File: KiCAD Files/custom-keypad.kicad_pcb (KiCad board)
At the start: 2 copper layers, 67.8 x 65.6 mm, 50 parts, among them IC1 AZ1117IH-3.3TRG1, IC2 USBLC6-2SC6, J1 UJ32-C-H-G-H2-SMT-TR, J2 EN11-HSM1BF20, J3 61300511121, SW1 SW_Push, SW2 SW_Push, SW3 SW_Push, SW4 SW_Push, SW8 SW_Push, SW9 SW_Push, U1 STM32H7A3RGTx, Y2 XRCGB25M000FAN00R0

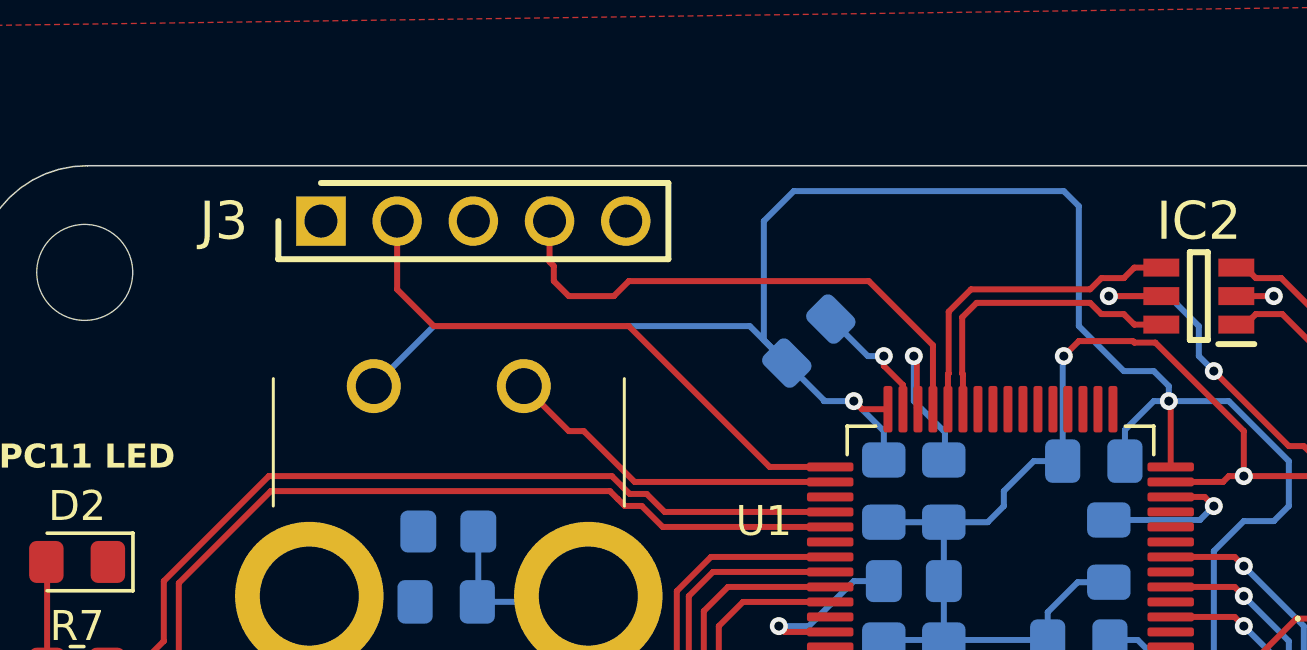
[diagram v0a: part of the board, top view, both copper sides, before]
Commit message: adjusted programming header location to provide more space to dial
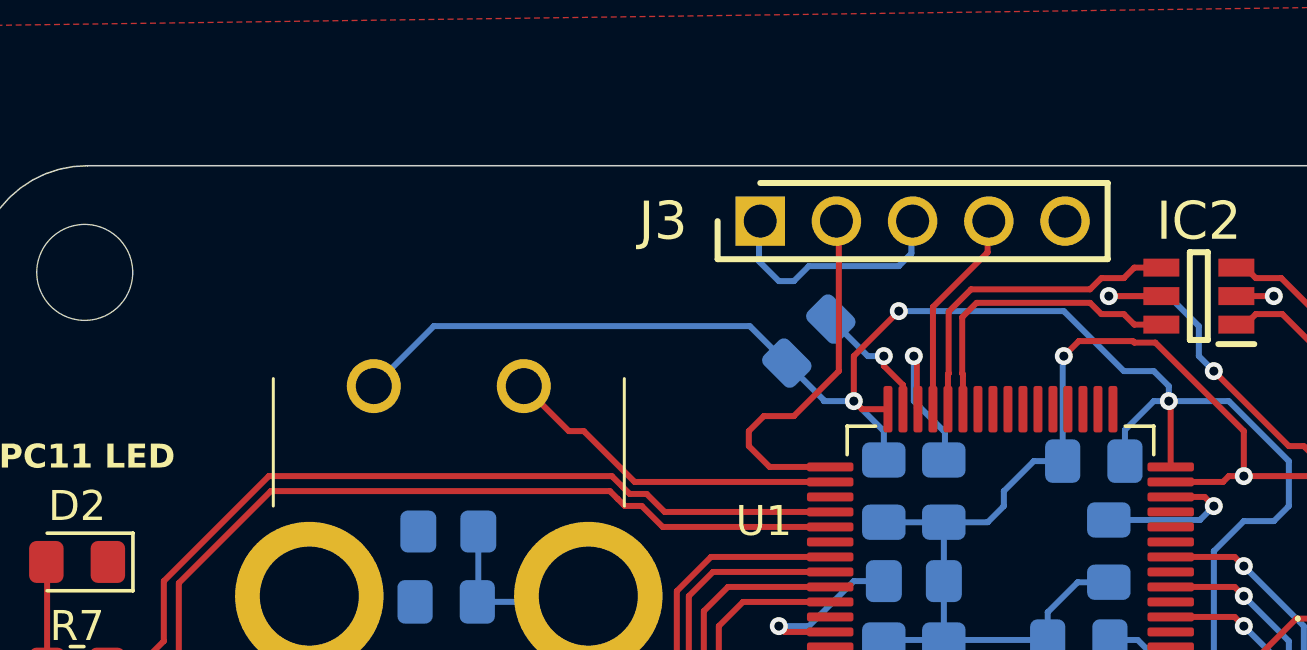
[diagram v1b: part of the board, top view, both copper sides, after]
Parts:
- moved J3 14.6 mm to (77.4, 27.5)
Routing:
- net PA13/SWDIO: track 18.1 -> 7.02 mm
- net VBAT: track 254.6 -> 244.3 mm, vias 7 -> 8
- net GND: track 146.5 -> 154.6 mm
- net PA14/SWCLK: track 19.2 -> 12.4 mm
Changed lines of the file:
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@@
 	(footprint "CustomFootprints:HDRV5W64P0X254_1X5_1270X254X854P"
 		(layer "F.Cu")
-		(at 62.738 27.5)
+		(at 77.38 27.5)
 		(descr "61300511121-1")
 		(tags "Connector")
@@
 	)
 	(segment
+		(start 78.5 29.5)
+		(end 78 29.5)
+		(width 0.2)
+		(layer "B.Cu")
+		(net 1)
+	)
+	(segment
 		(start 113.5 34)
 		(end 113.5 38)
@@
 	)
 	(segment
+		(start 78 29.5)
+		(end 77.34 28.84)
+		(width 0.2)
+		(layer "B.Cu")
+		(net 1)
+	)
+	(segment
 		(start 78 43.5)
 		(end 77.5 44)
@@
 	)
 	(segment
+		(start 82.42 27.5)
+		(end 82.42 28.58)
+		(width 0.2)
+		(layer "B.Cu")
+		(net 1)
+	)
+	(segment
 		(start 86.9625 40.5375)
 		(end 87.9625 39.5375)
@@
 	)
 	(segment
+		(start 79 29)
+		(end 78.5 29.5)
+		(width 0.2)
+		(layer "B.Cu")
+		(net 1)
+	)
+	(segment
 		(start 86.9625 46.4625)
 		(end 87 46.5)
@@
 	)
 	(segment
+		(start 82 29)
+		(end 79 29)
+		(width 0.2)
+		(layer "B.Cu")
+		(net 1)
+	)
+	(segment
 		(start 87.9625 39.5375)
 		(end 89 39.5375)
@@
 	)
 	(segment
+		(start 82.42 28.58)
+		(end 82 29)
+		(width 0.2)
+		(layer "B.Cu")
+		(net 1)
+	)
+	(segment
+		(start 77.34 28.84)
+		(end 77.34 27.5)
+		(width 0.2)
+		(layer "B.Cu")
+		(net 1)
+	)
+	(segment
 		(start 106.742 77.724)
 		(end 87.842 77.724)
@@
 	)
 	(segment
+		(start 80.5 32)
+		(end 80.5 33.5)
+		(width 0.2)
+		(layer "F.Cu")
+		(net 2)
+	)
+	(segment
 		(start 88.944213 47.233623)
 		(end 87.638 45.92741)
@@
 	)
 	(segment
+		(start 82 30.5)
+		(end 80.5 32)
+		(width 0.2)
+		(layer "F.Cu")
+		(net 2)
+	)
+	(segment
 		(start 91.063 33.563)
 		(end 91.063 35.695)
@@
 	)
 	(via
+		(at 82 30.5)
+		(size 0.6)
+		(drill 0.3)
+		(layers "F.Cu" "B.Cu")
+		(net 2)
+	)
+	(via
 		(at 89.233623 47.233623)
 		(size 0.6)
@@
 	)
 	(segment
-		(start 116.5 45.5)
-		(end 116.5 50.4)
+		(start 66.5 31)
+		(end 64.5 33)
 		(width 0.2)
 		(layer "B.Cu")
@@
 	)
 	(segment
-		(start 77.5 27.5)
-		(end 77.5 31.467246)
+		(start 116.5 45.5)
+		(end 116.5 50.4)
 		(width 0.2)
 		(layer "B.Cu")
@@
 	)
 	(segment
-		(start 88 31)
-		(end 88 27)
+		(start 78.266377 32.233623)
+		(end 77.032754 31)
 		(width 0.2)
 		(layer "B.Cu")
@@
 	)
 	(segment
+		(start 77.032754 31)
+		(end 66.5 31)
+		(width 0.2)
+		(layer "B.Cu")
+		(net 2)
+	)
+	(segment
 		(start 88.5 48)
 		(end 88.5 47.967246)
@@
 	)
 	(segment
-		(start 77.5 31.467246)
-		(end 78.266377 32.233623)
-		(width 0.2)
-		(layer "B.Cu")
-		(net 2)
-	)
-	(segment
 		(start 89.5375 35.5)
 		(end 89.5375 34.4625)
@@
 	)
 	(segment
-		(start 88 27)
-		(end 87.5 26.5)
-		(width 0.2)
-		(layer "B.Cu")
-		(net 2)
-	)
-	(segment
 		(start 90.595 42.095)
 		(end 89.9625 41.4625)
@@
 	)
 	(segment
-		(start 78.5 26.5)
-		(end 77.5 27.5)
-		(width 0.2)
-		(layer "B.Cu")
-		(net 2)
-	)
-	(segment
 		(start 87.5 48)
 		(end 88.5 48)
@@
 	)
 	(segment
+		(start 90.5 32.5)
+		(end 89.5 32.5)
+		(width 0.2)
+		(layer "B.Cu")
+		(net 2)
+	)
+	(segment
 		(start 105.5 51)
 		(end 105.5 54.5)
@@
 	)
 	(segment
-		(start 91 33)
-		(end 90.5 32.5)
-		(width 0.2)
-		(layer "B.Cu")
-		(net 2)
-	)
-	(segment
 		(start 85.5 44)
 		(end 85.5 46)
@@
 	)
 	(segment
-		(start 89.233623 47.233623)
-		(end 90.266377 47.233623)
-		(width 0.2)
-		(layer "B.Cu")
-		(net 2)
-	)
-	(segment
-		(start 90.5 32.5)
-		(end 89.5 32.5)
+		(start 91 33)
+		(end 90.5 32.5)
 		(width 0.2)
 		(layer "B.Cu")
@@
 	)
 	(segment
-		(start 91 33.5)
-		(end 91 33)
+		(start 89.233623 47.233623)
+		(end 90.266377 47.233623)
 		(width 0.2)
 		(layer "B.Cu")
@@
 	)
 	(segment
-		(start 66.5 31)
-		(end 64.5 33)
+		(start 87.5 30.5)
+		(end 82 30.5)
 		(width 0.2)
 		(layer "B.Cu")
@@
 	)
 	(segment
-		(start 87.5 26.5)
-		(end 78.5 26.5)
-		(width 0.2)
-		(layer "B.Cu")
-		(net 2)
-	)
-	(segment
-		(start 78.266377 32.233623)
-		(end 77.032754 31)
-		(width 0.2)
-		(layer "B.Cu")
-		(net 2)
-	)
-	(segment
 		(start 92.5 38.5)
 		(end 93.5 37.5)
@@
 	)
 	(segment
-		(start 79.733623 46.733623)
-		(end 80.5 47.5)
-		(width 0.2)
-		(layer "B.Cu")
-		(net 2)
-	)
-	(segment
-		(start 77.032754 31)
-		(end 66.5 31)
+		(start 89.5 32.5)
+		(end 87.5 30.5)
 		(width 0.2)
 		(layer "B.Cu")
@@
 	)
 	(segment
-		(start 89.5 32.5)
-		(end 88 31)
+		(start 79.733623 46.733623)
+		(end 80.5 47.5)
 		(width 0.2)
 		(layer "B.Cu")
@@
 	)
 	(segment
+		(start 91 33.5)
+		(end 91 33)
+		(width 0.2)
+		(layer "B.Cu")
+		(net 2)
+	)
+	(segment
 		(start 80.5 33.5)
 		(end 79.5 33.5)
@@
 	)
 	(segment
-		(start 70.5 29.5)
-		(end 70.5 29)
-		(width 0.2)
-		(layer "F.Cu")
-		(net 12)
-	)
-	(segment
-		(start 70.358 28.858)
-		(end 70.358 27.5)
-		(width 0.2)
-		(layer "F.Cu")
-		(net 12)
-	)
-	(segment
-		(start 71 30)
-		(end 70.5 29.5)
-		(width 0.2)
-		(layer "F.Cu")
-		(net 12)
-	)
-	(segment
-		(start 81 29.5)
-		(end 73 29.5)
-		(width 0.2)
-		(layer "F.Cu")
-		(net 12)
-	)
-	(segment
-		(start 73 29.5)
-		(end 72.5 30)
-		(width 0.2)
-		(layer "F.Cu")
-		(net 12)
-	)
-	(segment
-		(start 83.138 31.638)
-		(end 81 29.5)
-		(width 0.2)
-		(layer "F.Cu")
-		(net 12)
-	)
-	(segment
-		(start 70.5 29)
-		(end 70.358 28.858)
+		(start 83.138 33.77)
+		(end 83.138 30.362)
 		(width 0.2)
 		(layer "F.Cu")
@@
 	)
 	(segment
-		(start 83.138 33.77)
-		(end 83.138 31.638)
+		(start 84.96 28.54)
+		(end 84.96 27.5)
 		(width 0.2)
 		(layer "F.Cu")
@@
 	)
 	(segment
-		(start 72.5 30)
-		(end 71 30)
+		(start 83.138 30.362)
+		(end 84.96 28.54)
 		(width 0.2)
 		(layer "F.Cu")
@@
 	)
 	(segment
-		(start 66.5 31)
-		(end 65.278 29.778)
+		(start 77.695 35.695)
+		(end 77 35)
 		(width 0.2)
 		(layer "F.Cu")
@@
 	)
 	(segment
-		(start 73 31)
-		(end 66.5 31)
+		(start 77 34.5)
+		(end 77.5 34)
+		(width 0.2)
+		(layer "F.Cu")
+		(net 14)
+	)
+	(segment
+		(start 77.5 34)
+		(end 78.5 34)
+		(width 0.2)
+		(layer "F.Cu")
+		(net 14)
+	)
+	(segment
+		(start 80 27.62)
+		(end 79.88 27.5)
+		(width 0.2)
+		(layer "F.Cu")
+		(net 14)
+	)
+	(segment
+		(start 80 32.5)
+		(end 80 27.62)
 		(width 0.2)
 		(layer "F.Cu")
@@
 	)
 	(segment
-		(start 65.278 29.778)
-		(end 65.278 27.5)
+		(start 78.5 34)
+		(end 80 32.5)
 		(width 0.2)
 		(layer "F.Cu")
@@
 	)
 	(segment
-		(start 77.695 35.695)
-		(end 73 31)
+		(start 77 35)
+		(end 77 34.5)
 		(width 0.2)
 		(layer "F.Cu")
@@
 			)
 		)
+	)
+	(zone
+		(net 0)
+		(net_name "")
+		(layers "F&B.Cu")
+		(hatch edge 0.5)
+		(connect_pads
+			(clearance 0)
+		)
+		(min_thickness 0.25)
+		(filled_areas_thickness no)
+		(keepout
+			(tracks allowed)
+			(vias allowed)
+			(pads allowed)
+			(copperpour not_allowed)
+			(footprints allowed)
+		)
+		(fill
+			(thermal_gap 0.5)
+			(thermal_bridge_width 0.5)
+		)
+		(polygon
+			(pts
+				(xy 76 26) (xy 75.853553 29) (xy 79 29) (xy 79 26)
+			)
+		)

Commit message: retrieved older pcb files that were manufactured
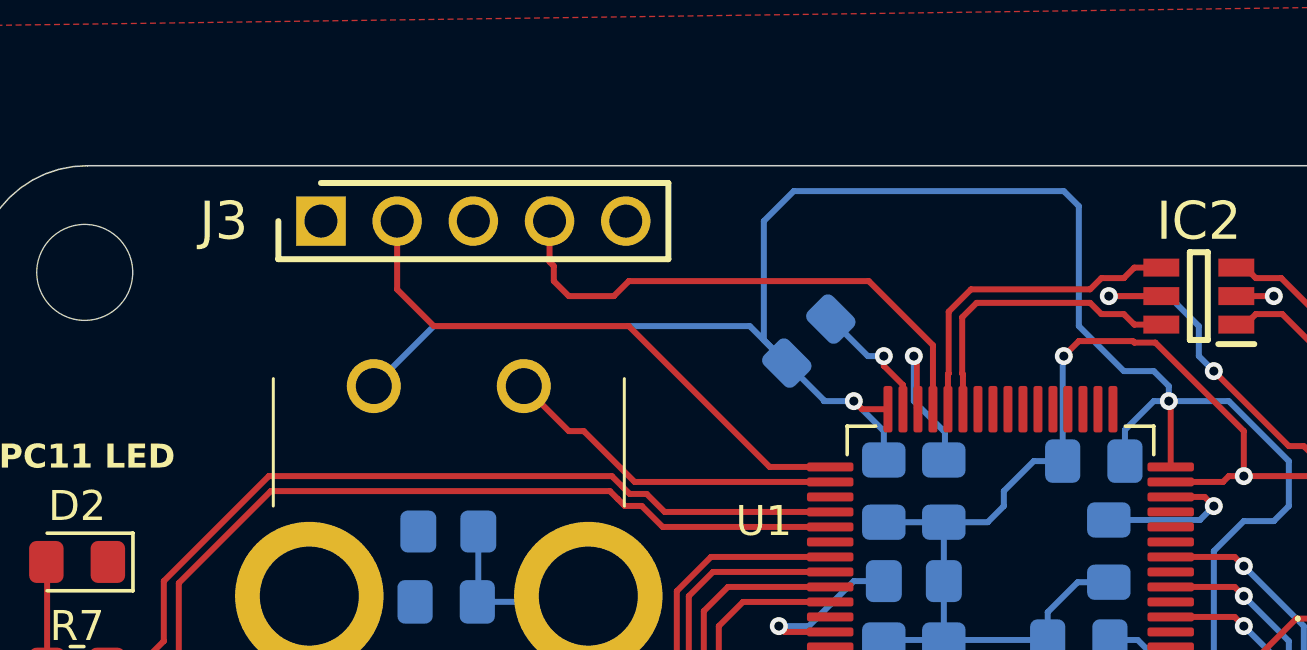
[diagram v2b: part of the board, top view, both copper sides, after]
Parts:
- moved J3 14.6 mm to (62.7, 27.5)
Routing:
- net PA13/SWDIO: track 7.02 -> 18.1 mm
- net VBAT: track 244.3 -> 254.6 mm, vias 8 -> 7
- net GND: track 154.6 -> 146.5 mm
- net PA14/SWCLK: track 12.4 -> 19.2 mm
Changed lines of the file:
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@@
 			(drillshape 0)
 			(scaleselection 1)
-			(outputdirectory "C:/Users/Jay62/570proj/custom-keypad/KiCAD Files/Gerber Files/")
+			(outputdirectory "Gerber Files/")
 		)
 	)
@@
 	(footprint "CustomFootprints:HDRV5W64P0X254_1X5_1270X254X854P"
 		(layer "F.Cu")
-		(at 77.38 27.5)
+		(at 62.738 27.5)
 		(descr "61300511121-1")
 		(tags "Connector")
@@
 	)
 	(segment
-		(start 78.5 29.5)
-		(end 78 29.5)
-		(width 0.2)
-		(layer "B.Cu")
-		(net 1)
-	)
-	(segment
 		(start 113.5 34)
 		(end 113.5 38)
@@
 	)
 	(segment
-		(start 78 29.5)
-		(end 77.34 28.84)
-		(width 0.2)
-		(layer "B.Cu")
-		(net 1)
-	)
-	(segment
 		(start 78 43.5)
 		(end 77.5 44)
@@
 	)
 	(segment
-		(start 82.42 27.5)
-		(end 82.42 28.58)
-		(width 0.2)
-		(layer "B.Cu")
-		(net 1)
-	)
-	(segment
 		(start 86.9625 40.5375)
 		(end 87.9625 39.5375)
@@
 	)
 	(segment
-		(start 79 29)
-		(end 78.5 29.5)
-		(width 0.2)
-		(layer "B.Cu")
-		(net 1)
-	)
-	(segment
 		(start 86.9625 46.4625)
 		(end 87 46.5)
@@
 	)
 	(segment
-		(start 82 29)
-		(end 79 29)
-		(width 0.2)
-		(layer "B.Cu")
-		(net 1)
-	)
-	(segment
 		(start 87.9625 39.5375)
 		(end 89 39.5375)
@@
 	)
 	(segment
-		(start 82.42 28.58)
-		(end 82 29)
-		(width 0.2)
-		(layer "B.Cu")
-		(net 1)
-	)
-	(segment
-		(start 77.34 28.84)
-		(end 77.34 27.5)
-		(width 0.2)
-		(layer "B.Cu")
-		(net 1)
-	)
-	(segment
 		(start 106.742 77.724)
 		(end 87.842 77.724)
@@
 	)
 	(segment
-		(start 80.5 32)
-		(end 80.5 33.5)
-		(width 0.2)
-		(layer "F.Cu")
-		(net 2)
-	)
-	(segment
 		(start 88.944213 47.233623)
 		(end 87.638 45.92741)
@@
 	)
 	(segment
-		(start 82 30.5)
-		(end 80.5 32)
-		(width 0.2)
-		(layer "F.Cu")
-		(net 2)
-	)
-	(segment
 		(start 91.063 33.563)
 		(end 91.063 35.695)
@@
 	)
 	(via
-		(at 82 30.5)
-		(size 0.6)
-		(drill 0.3)
-		(layers "F.Cu" "B.Cu")
-		(net 2)
-	)
-	(via
 		(at 89.233623 47.233623)
 		(size 0.6)
@@
 	)
 	(segment
-		(start 66.5 31)
-		(end 64.5 33)
+		(start 116.5 45.5)
+		(end 116.5 50.4)
 		(width 0.2)
 		(layer "B.Cu")
@@
 	)
 	(segment
-		(start 116.5 45.5)
-		(end 116.5 50.4)
+		(start 77.5 27.5)
+		(end 77.5 31.467246)
 		(width 0.2)
 		(layer "B.Cu")
@@
 	)
 	(segment
-		(start 78.266377 32.233623)
-		(end 77.032754 31)
+		(start 88 31)
+		(end 88 27)
 		(width 0.2)
 		(layer "B.Cu")
@@
 	)
 	(segment
-		(start 77.032754 31)
-		(end 66.5 31)
-		(width 0.2)
-		(layer "B.Cu")
-		(net 2)
-	)
-	(segment
 		(start 88.5 48)
 		(end 88.5 47.967246)
@@
 	)
 	(segment
+		(start 77.5 31.467246)
+		(end 78.266377 32.233623)
+		(width 0.2)
+		(layer "B.Cu")
+		(net 2)
+	)
+	(segment
 		(start 89.5375 35.5)
 		(end 89.5375 34.4625)
@@
 	)
 	(segment
+		(start 88 27)
+		(end 87.5 26.5)
+		(width 0.2)
+		(layer "B.Cu")
+		(net 2)
+	)
+	(segment
 		(start 90.595 42.095)
 		(end 89.9625 41.4625)
@@
 	)
 	(segment
+		(start 78.5 26.5)
+		(end 77.5 27.5)
+		(width 0.2)
+		(layer "B.Cu")
+		(net 2)
+	)
+	(segment
 		(start 87.5 48)
 		(end 88.5 48)
@@
 	)
 	(segment
-		(start 90.5 32.5)
-		(end 89.5 32.5)
-		(width 0.2)
-		(layer "B.Cu")
-		(net 2)
-	)
-	(segment
 		(start 105.5 51)
 		(end 105.5 54.5)
@@
 	)
 	(segment
+		(start 91 33)
+		(end 90.5 32.5)
+		(width 0.2)
+		(layer "B.Cu")
+		(net 2)
+	)
+	(segment
 		(start 85.5 44)
 		(end 85.5 46)
@@
 	)
 	(segment
-		(start 91 33)
-		(end 90.5 32.5)
+		(start 89.233623 47.233623)
+		(end 90.266377 47.233623)
 		(width 0.2)
 		(layer "B.Cu")
@@
 	)
 	(segment
-		(start 89.233623 47.233623)
-		(end 90.266377 47.233623)
+		(start 90.5 32.5)
+		(end 89.5 32.5)
+		(width 0.2)
+		(layer "B.Cu")
+		(net 2)
+	)
+	(segment
+		(start 91 33.5)
+		(end 91 33)
 		(width 0.2)
 		(layer "B.Cu")
@@
 	)
 	(segment
-		(start 87.5 30.5)
-		(end 82 30.5)
+		(start 66.5 31)
+		(end 64.5 33)
 		(width 0.2)
 		(layer "B.Cu")
@@
 	)
 	(segment
-		(start 92.5 38.5)
-		(end 93.5 37.5)
+		(start 87.5 26.5)
+		(end 78.5 26.5)
 		(width 0.2)
 		(layer "B.Cu")
@@
 	)
 	(segment
-		(start 89.5 32.5)
-		(end 87.5 30.5)
+		(start 78.266377 32.233623)
+		(end 77.032754 31)
+		(width 0.2)
+		(layer "B.Cu")
+		(net 2)
+	)
+	(segment
+		(start 92.5 38.5)
+		(end 93.5 37.5)
 		(width 0.2)
 		(layer "B.Cu")
@@
 	)
 	(segment
+		(start 77.032754 31)
+		(end 66.5 31)
+		(width 0.2)
+		(layer "B.Cu")
+		(net 2)
+	)
+	(segment
+		(start 89.5 32.5)
+		(end 88 31)
+		(width 0.2)
+		(layer "B.Cu")
+		(net 2)
+	)
+	(segment
 		(start 80.4625 43.5375)
 		(end 79.75 44.25)
@@
 	)
 	(segment
-		(start 91 33.5)
-		(end 91 33)
-		(width 0.2)
-		(layer "B.Cu")
-		(net 2)
-	)
-	(segment
 		(start 80.5 33.5)
 		(end 79.5 33.5)
@@
 	)
 	(segment
-		(start 83.138 33.77)
-		(end 83.138 30.362)
+		(start 70.5 29.5)
+		(end 70.5 29)
+		(width 0.2)
+		(layer "F.Cu")
+		(net 12)
+	)
+	(segment
+		(start 70.358 28.858)
+		(end 70.358 27.5)
+		(width 0.2)
+		(layer "F.Cu")
+		(net 12)
+	)
+	(segment
+		(start 71 30)
+		(end 70.5 29.5)
+		(width 0.2)
+		(layer "F.Cu")
+		(net 12)
+	)
+	(segment
+		(start 81 29.5)
+		(end 73 29.5)
 		(width 0.2)
 		(layer "F.Cu")
@@
 	)
 	(segment
-		(start 84.96 28.54)
-		(end 84.96 27.5)
+		(start 73 29.5)
+		(end 72.5 30)
 		(width 0.2)
 		(layer "F.Cu")
@@
 	)
 	(segment
-		(start 83.138 30.362)
-		(end 84.96 28.54)
+		(start 83.138 31.638)
+		(end 81 29.5)
+		(width 0.2)
+		(layer "F.Cu")
+		(net 12)
+	)
+	(segment
+		(start 70.5 29)
+		(end 70.358 28.858)
+		(width 0.2)
+		(layer "F.Cu")
+		(net 12)
+	)
+	(segment
+		(start 83.138 33.77)
+		(end 83.138 31.638)
+		(width 0.2)
+		(layer "F.Cu")
+		(net 12)
+	)
+	(segment
+		(start 72.5 30)
+		(end 71 30)
 		(width 0.2)
 		(layer "F.Cu")
@@
 	)
 	(segment
-		(start 77.695 35.695)
-		(end 77 35)
-		(width 0.2)
-		(layer "F.Cu")
-		(net 14)
-	)
-	(segment
-		(start 77 34.5)
-		(end 77.5 34)
-		(width 0.2)
-		(layer "F.Cu")
-		(net 14)
-	)
-	(segment
-		(start 77.5 34)
-		(end 78.5 34)
-		(width 0.2)
-		(layer "F.Cu")
-		(net 14)
-	)
-	(segment
-		(start 80 27.62)
-		(end 79.88 27.5)
+		(start 66.5 31)
+		(end 65.278 29.778)
 		(width 0.2)
 		(layer "F.Cu")
@@
 	)
 	(segment
-		(start 80 32.5)
-		(end 80 27.62)
+		(start 73 31)
+		(end 66.5 31)
 		(width 0.2)
 		(layer "F.Cu")
@@
 	)
 	(segment
-		(start 78.5 34)
-		(end 80 32.5)
+		(start 65.278 29.778)
+		(end 65.278 27.5)
 		(width 0.2)
 		(layer "F.Cu")
@@
 	)
 	(segment
-		(start 77 35)
-		(end 77 34.5)
+		(start 77.695 35.695)
+		(end 73 31)
 		(width 0.2)
 		(layer "F.Cu")
@@
 			)
 		)
-	)
-	(zone
-		(net 0)
-		(net_name "")
-		(layers "F&B.Cu")
-		(hatch edge 0.5)
-		(connect_pads
-			(clearance 0)
-		)
-		(min_thickness 0.25)
-		(filled_areas_thickness no)
-		(keepout
-			(tracks allowed)
-			(vias allowed)
-			(pads allowed)
-			(copperpour not_allowed)
-			(footprints allowed)
-		)
-		(fill
-			(thermal_gap 0.5)
-			(thermal_bridge_width 0.5)
-		)
-		(polygon
-			(pts
-				(xy 76 26) (xy 75.853553 29) (xy 79 29) (xy 79 26)
-			)
-		)
